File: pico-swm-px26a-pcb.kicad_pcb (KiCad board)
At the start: 2 copper layers, 62 x 58 mm, 12 parts, among them J1 Conn_01x03, J2 STLZ950/3G-5.08-V-GRÜN, U1 Pico, U2 4N35

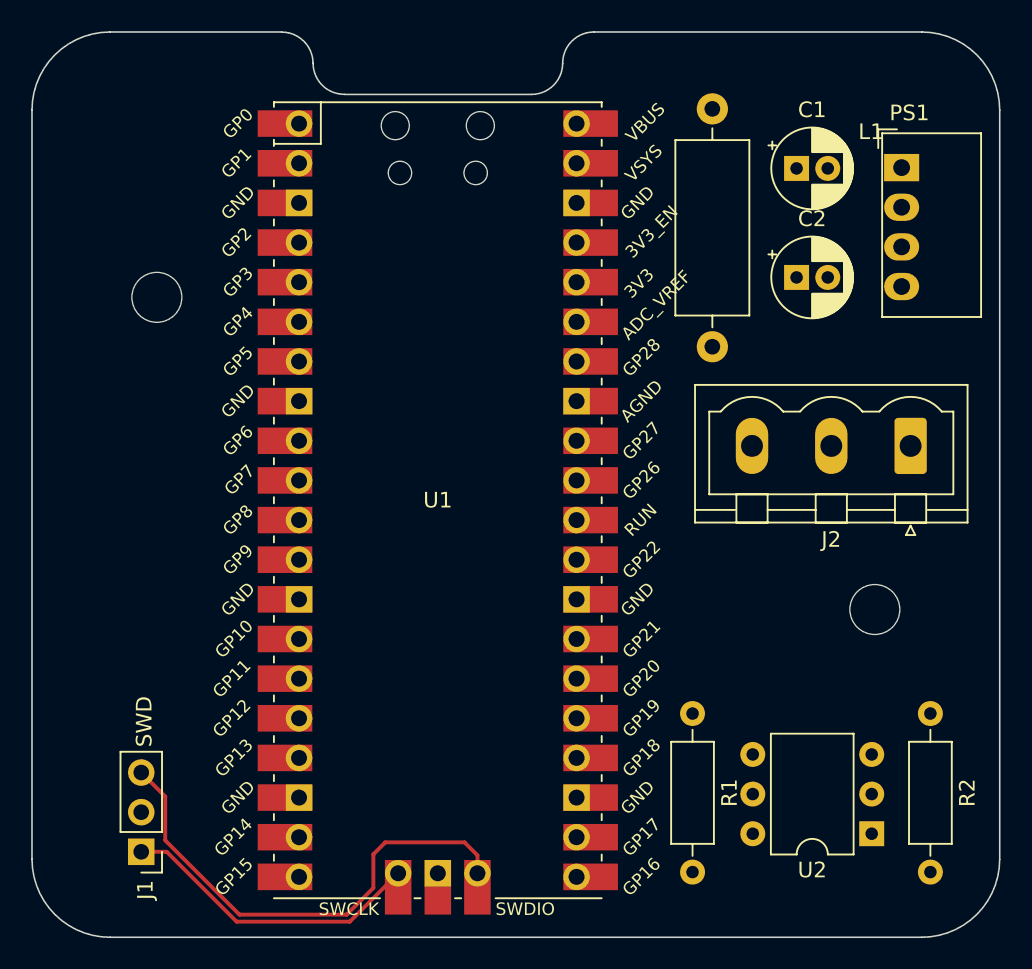
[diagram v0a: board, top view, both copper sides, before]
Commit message: Add EEPROM
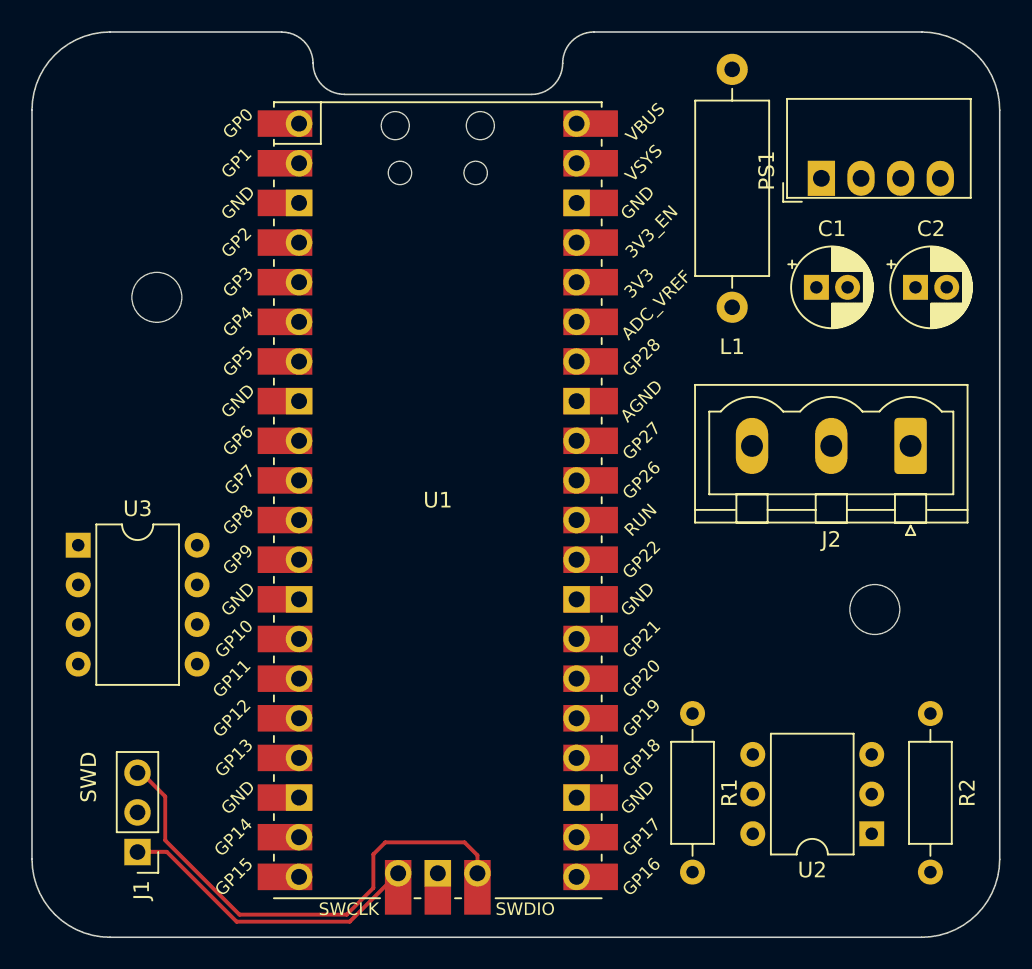
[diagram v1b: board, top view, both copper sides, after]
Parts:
- added U3: 25LCxxx, Package_DIP:DIP-8_W7.62mm, F.Cu at (108.0, 102.9)
- moved L1 12.8 mm to (149.9, 87.6), turned to 90 degrees
- moved C1 7.73 mm to (155.3, 86.4)
- moved C2 7.65 mm to (161.6, 86.4)
- moved PS1 5.19 mm to (155.6, 79.4), turned to 90 degrees
- moved J1 0.24 mm to (111.8, 122.5)
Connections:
- U1 pad 10: unconnected-(U1-GPIO7-Pad10) -> Net-(U1-GPIO7)
- U1 pad 11: unconnected-(U1-GPIO8-Pad11) -> Net-(U1-GPIO8)
- U1 pad 12: unconnected-(U1-GPIO9-Pad12) -> Net-(U1-GPIO9)
- U1 pad 14: unconnected-(U1-GPIO10-Pad14) -> Net-(U1-GPIO10)
- U1 pad 15: unconnected-(U1-GPIO11-Pad15) -> Net-(U1-GPIO11)
- U1 pad 16: unconnected-(U1-GPIO12-Pad16) -> Net-(U1-GPIO12)

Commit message: Add EEPROM cap
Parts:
- added C3: 33u, Capacitor_THT:CP_Radial_D5.0mm_P2.00mm, F.Cu at (112.7, 96.5)

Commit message: Initial routing
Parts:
- added REF**: OSHW-Logo2_7.3x6mm_Copper, Symbol:OSHW-Logo2_7.3x6mm_Copper, F.Cu at (113.0, 78.0)
- moved L1 2.49 mm to (149.9, 90.1)
- moved C3 1.27 mm to (112.7, 97.8)
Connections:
- U1 pad 10: Net-(U1-GPIO7) -> unconnected-(U1-GPIO7-Pad10)
- U1 pad 17: unconnected-(U1-GPIO13-Pad17) -> Net-(U1-GPIO13)
- U3 pad 1: Net-(U1-GPIO7) -> Net-(U1-GPIO13)
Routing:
- net +3V3: track 0.00 -> 95.3 mm
- net +12V: track 0.00 -> 54.7 mm
- net Net-(J2-Pin_1): track 0.00 -> 34.2 mm
- net +5V: track 0.00 -> 28.3 mm
- net Net-(U1-GPIO13): track 0.00 -> 26.8 mm
- net Net-(U1-GPIO12): track 0.00 -> 19.8 mm
- net Net-(U1-GPIO8): track 0.00 -> 16.8 mm
- net Net-(U1-GPIO16): track 0.00 -> 14.2 mm
- net Net-(PS1-+Vin): track 0.00 -> 10.9 mm
- net Net-(U1-GPIO9): track 0.00 -> 7.20 mm
- net Net-(U1-GPIO11): track 0.00 -> 6.92 mm
- net Net-(U1-GPIO10): track 0.00 -> 6.92 mm
- added copper zone on B.Cu, net GNDA
- added copper zone on F.Cu, net GNDA
- added copper zone on B.Cu, net GNDD
- added copper zone on F.Cu, net GNDD
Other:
- board text added: "(C) Sergej Sawazki 2023"
- board text added: "BK"
- board text added: "BL"
- board text added: "BR"
- board text added: "DEBUG"
- board text added: "EX-26A"
- board text added: "OR"
- board text added: "V1.0"
- board text added: "YL"
- board text added: "pico-swm-ex26a"
- board text removed: "SWD"
